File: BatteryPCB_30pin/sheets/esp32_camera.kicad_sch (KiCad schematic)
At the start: 10 parts, among them J1 ESP32 left, J2 ESP32 right, J3 RunCam Split 4

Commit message: Battery PCB 30-pin: J3 pin order matches the RunCam Split 4 pads
J3 pins 3 and 5 swapped (3 = CAM_VIDEO, 5 = CAM_RX), so J3 pin 1..5 =
VCC, GND, Video, TX, RX, the camera's own pad order: the camera harness
is now a straight cable with no crossed wires.

- Schematic sheet 3 and the board pad nets updated; CAM_RX now drops to
  the back right beside pin 5 (route 2.5 mm shorter, old via removed).
- Back-silk legend reads 3 VID / 4 TX / 5 RX; README harness table, BOM
  camera note and hand-fit list updated; Gerbers, order-package zip,
  schematic PDF, project zip and STEP regenerated.
- ERC 0 errors, DRC 0 (schematic parity, zones refilled, same 3
  exclusions), verify_A unchanged, all 27 CPL placements re-checked.

BatteryPCB (the 38-pin board) keeps its old J3 order.

Co-Authored-By: Claude Opus 5.5 <noreply@anthropic.com>
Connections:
- net CAM_RX: now also J3.5 (Pin_5); no longer J3.3 (Pin_3)
- net CAM_VIDEO: now also J3.3 (Pin_3); no longer J3.5 (Pin_5)
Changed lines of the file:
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@@
 	(wire
 		(pts
-			(xy 189.23 104.14) (xy 236.22 104.14)
+			(xy 189.23 104.14) (xy 213.36 104.14)
 		)
 		(stroke
@@
 	)
 	(label "CAM_VIDEO"
-		(at 231.14 109.22 180)
+		(at 231.14 104.14 180)
 		(effects
 			(font
@@
 		)
 	)
+	(label "CAM_RX"
+		(at 231.14 109.22 180)
+		(effects
+			(font
+				(size 1.27 1.27)
+			)
+			(justify right bottom)
+		)
+	)
+	(wire
+		(pts
+			(xy 236.22 104.14) (xy 231.14 104.14)
+		)
+		(stroke
+			(width 0)
+			(type default)
+		)
+	)

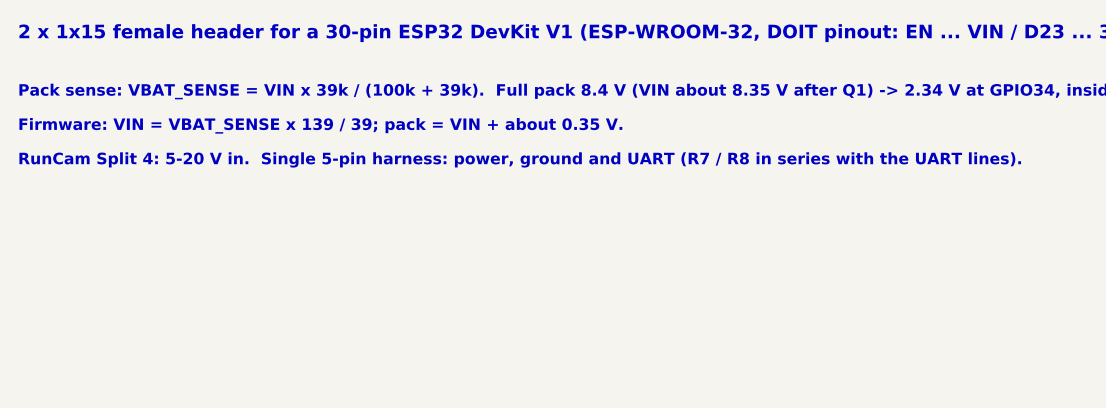
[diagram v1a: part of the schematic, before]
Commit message: Battery PCB 30-pin: XT30 and battery-holder holes to the datasheets; notes, check script
- XT30 J5/J6 pin holes 1.8 -> 1.9 mm (Amass drawing: 1.9 mm for the
  1.6 mm pins); 0.55 mm copper ring left on the 3.0 mm pads.
- Keystone 1042 holder peg holes 3.45 -> 3.5 mm and locator hole
  2.39 -> 2.4 mm on BT1-BT4 (Keystone M65p27; positions unchanged).
  Footprints updated in battery_pcb.pretty and on the board.
- Only those 16 hole sizes changed on the board: no part, trace, via,
  outline or silk moved. Tightest new gap: COTS_SW to a BT4 peg hole
  0.375 mm (rule 0.3).
- Schematic notes brought up to date: Q1 drop ~0.05 V (was 0.35 V from
  the old diode), J5/J6 are XT30 not Micro-Fit, C9/C10 sit at the
  ESP32's VIN (J1-15).
- verify_A: the old "seven edge cut-outs" count is replaced by a real
  check (7 rim notches + 4 square zip-tie cut-outs); ALL PASS, 36 checks.
- Gerbers, order-package zip, schematic PDF, project zip and STEP
  regenerated; BOM and CPL unchanged.

ERC 0 errors, DRC 0 (schematic parity, zones refilled, same 3
documented exclusions).

Co-Authored-By: Claude Opus 5.5 <noreply@anthropic.com>
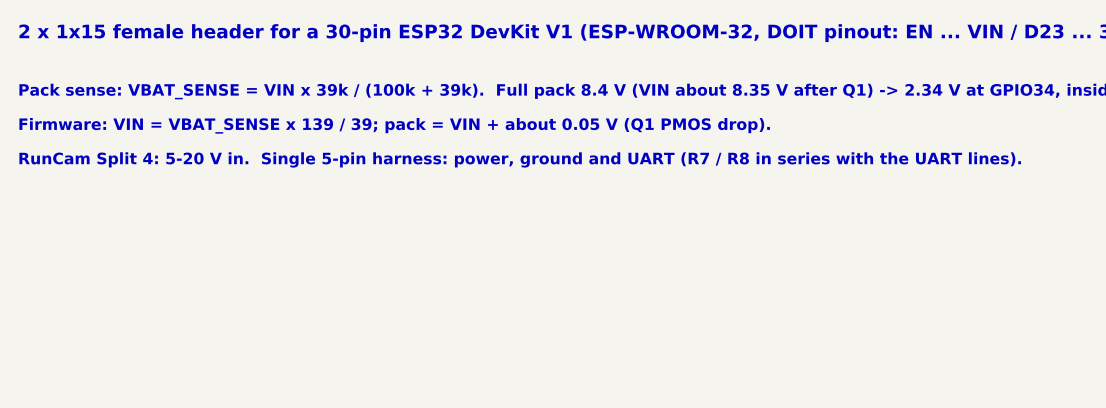
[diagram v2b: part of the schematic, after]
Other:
- note added: "Firmware: VIN = VBAT_SENSE x 139 / 39; pack = VIN + about 0.05 V (Q1 PMOS drop)."
- note removed: "Firmware: VIN = VBAT_SENSE x 139 / 39; pack = VIN + about 0.35 V."
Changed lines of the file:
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@@
 		(company "Stanford SSI")
 	)
-	(text "Firmware: VIN = VBAT_SENSE x 139 / 39; pack = VIN + about 0.35 V."
+	(text "Firmware: VIN = VBAT_SENSE x 139 / 39; pack = VIN + about 0.05 V (Q1 PMOS drop)."
 		(exclude_from_sim no)
 		(at 25.4 40.64 0)
